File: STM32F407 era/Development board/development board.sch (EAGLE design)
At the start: 59 parts, among them IC1 74HC595N, IC2 74HC595N, IC3 317T, IC4 317T, X1 K375M, X2 HD44780LCD-1602, X3 SDBMF

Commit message: Continued work on dev board layout
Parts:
- added H1, H2, H3: MOUNT-HOLE3.2, holes:MOUNT-HOLE3.2
- added ISP1: AVRISP-BOX, adafruit:AVRISP-BOX
- added JP1: USB_MICROB_PLUGCONN-11752, SparkFun-Connectors:USB_MICROB_PLUGCONN-11752
- added JP2: (no value), microbuilder:HEADER-1X2ROUND
- added R28: 1k8, microbuilder:RESISTOR_0603
- added SV1: (no value), con-lstb:MA08-1
- added SV2, SV3, SV4: (no value), con-lstb:MA03-1
- added U$57: MICROFIT4, unicorn:MICROFIT4
- added U1: MAX13052ESA+, Maxim_By_element14_Batch_1:MAX13052ESA+
- added X4, X8, X9: 057-006-1, con-panduit:057-006-1
- R2: value (none) -> 732
- R4: value (none) -> 400
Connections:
- removed net N$20: U$1G$3.PB7
- removed net N$33: U$1G$2.PB12
- new net CANH: R28.2, U$57.PIN1, U1.CANH
- new net CANL: R28.1, U$57.PIN2, U1.CANL
- new net CAN_RX: U$1G$3.PB5, U1.TXD
- new net CAN_TX: U$1G$3.PB6, U1.RXD
- new net D+: JP1.D+, U$1G$2.PB15
- new net D-: JP1.D-, U$1G$2.PB14
- new net DAC: JP2.2, U$1G$1.PA4
- new net SCL: SV4.2, U$1G$3.PB8, X9-3.S, X9-4.S
- new net SDA: SV4.1, U$1G$3.PB7, X9-5.S, X9-6.S
- new net SHIFTREG_LATCH: IC1A.RCK, IC2A.RCK
- new net SPI_MISO: ISP1.MISO, U$1G$1.PA6
- new net SPI_MOSI: IC1A.SER, ISP1.MOSI, U$1G$1.PA7
- new net SPI_SCK: IC1A.SCK, IC2A.SCK, ISP1.SCK, U$1G$1.PA5
- new net USART1_RX: SV2.2, U$1G$1.PB11, X4-3.S, X4-4.S
- new net USART1_TX: SV2.1, U$1G$1.PB10, X4-5.S, X4-6.S
- new net USART2_RX: SV3.2, U$1G$3.PD6, X8-3.S, X8-4.S
- new net USART2_TX: SV3.1, U$1G$3.PD5, X8-5.S, X8-6.S
- net 3.3V: now also IC1A.SCL, IC2A.SCL, ISP1.VCC, U1.VCC
- net E: now also U$1G$2.PC7; no longer U$1G$2.PB15
- net GND: now also IC1A.G, IC2A.G, ISP1.GND, JP1.GND, JP1.SHIELD, JP2.1, SV2.3, SV3.3, SV4.3, U$57.PIN3, U$57.PIN4, U1.GND, U1.RS, X4-1.S, X4-2.S, X8-1.S, X8-2.S, X9-1.S, X9-2.S
- net LED1: now also SV1.1, U$1G$1.PC4
- net LED2: now also SV1.2, U$1G$1.PC5
- net LED3: now also SV1.3, U$1G$1.PB0
- net LED4: now also SV1.4, U$1G$1.PB1
- net LED5: now also SV1.5, U$1G$1.PE7
- net LED6: now also SV1.6, U$1G$1.PA3
- net LED7: now also SV1.7, U$1G$2.PB12
- net LED8: now also SV1.8, U$1G$2.PA8
- net RW: now also U$1G$2.PC6; no longer U$1G$2.PB14
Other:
- note added: "DAC"
- note added: "I2C"
- note added: "USART1"
- note added: "USART2"
- moved on the sheet: C1, DIS2, IC2, IC2P, R5

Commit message: updates to the layout and done routing (maybe)
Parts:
- added JP3: (no value), pinhead:PINHD-2X11
- added LED10, LED9: (no value), led:LED3MM
- added R29: 150, microbuilder:RESISTOR_0603
- added R30: 100, microbuilder:RESISTOR_0603
- added SV5: (no value), con-lstb:MA03-2
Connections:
- new net N$20: LED10.A, R30.1
- new net N$31: LED9.A, R29.1
- new net PA0: JP3.4, U$1G$4.PA0
- new net PA1: JP3.3, U$1G$4.PA1
- new net PA2: JP3.2, U$1G$4.PA2
- new net PA9: JP3.1, U$1G$2.PA9
- new net PB4: JP3.18, U$1G$3.PB4
- new net PB9: JP3.17, U$1G$3.PB9
- new net PC0: JP3.8, U$1G$4.PC0
- new net PC1: JP3.7, U$1G$4.PC1
- new net PC13: JP3.9, U$1G$4.PC13
- new net PC2: JP3.6, U$1G$4.PC2
- new net PC3: JP3.5, U$1G$4.PC3
- new net PD4: JP3.20, U$1G$3.PD4
- new net PD7: JP3.19, U$1G$3.PD7
- new net PE0: JP3.16, U$1G$3.PE0
- new net PE1: JP3.15, U$1G$3.PE1
- new net PE2: JP3.14, U$1G$4.PE2
- new net PE3: JP3.13, U$1G$4.PE3
- new net PE4: JP3.12, U$1G$4.PE4
- new net PE5: JP3.11, U$1G$4.PE5
- new net PE6: JP3.10, U$1G$4.PE6
- net 3.3V: now also R30.2, SV5.2
- net 5.0V: now also R29.2
- net GND: now also JP3.21, JP3.22, LED10.C, LED9.C, SV5.6
- net SPI_MISO: now also SV5.1
- net SPI_MOSI: now also SV5.4
- net SPI_SCK: now also SV5.3
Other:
- moved on the sheet: C1, C2, C3, C4, C5, C6, DIS1, DIS2, IC1, IC1P, IC2, IC2P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

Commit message: fixed errors on dev board
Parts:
- removed JP1: USB_MICROB_PLUGCONN-11752, SparkFun-Connectors:USB_MICROB_PLUGCONN-11752
- added X5: PN61729-S, con-berg:PN61729-S
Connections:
- removed net SHIFTREG_LATCH: IC1A.RCK, IC2A.RCK
- net D+: now also X5.3; no longer JP1.D+
- net D-: now also X5.2; no longer JP1.D-
- net GND: now also X3.3, X5.4, X5.S1, X5.S2; no longer JP1.GND, JP1.SHIELD, X3.9
- net PA9: now also IC1A.RCK, IC2A.RCK
- net SDIO_CMD: now also R7.1, X3.2; no longer R8.1, X3.3
- net SDIO_D0: now also R8.1; no longer R9.1
- net SDIO_D1: now also R9.1; no longer R10.1
- net SDIO_D2: now also R10.1, X3.9; no longer R6.1, X3.1
- net SDIO_D3: now also R6.1, X3.1; no longer R7.1, X3.2

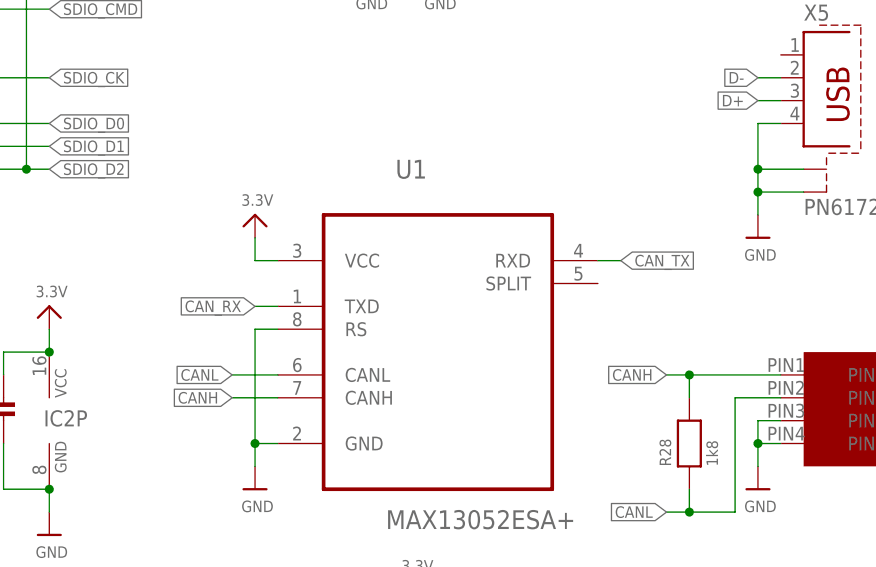
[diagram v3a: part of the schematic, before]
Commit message: fixed CAN controller connections
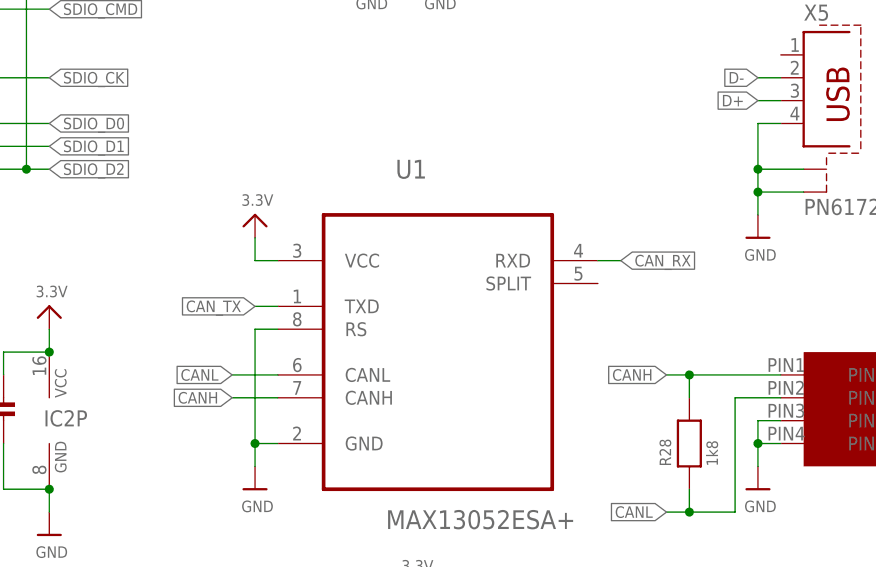
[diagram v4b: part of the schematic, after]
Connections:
- net CAN_RX: now also U1.RXD; no longer U1.TXD
- net CAN_TX: now also U1.TXD; no longer U1.RXD
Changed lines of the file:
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@@
 </segment>
 <segment>
-<pinref part="U1" gate="A" pin="TXD"/>
-<wire x1="203.2" y1="-48.26" x2="200.66" y2="-48.26" width="0.1524" layer="91"/>
-<label x="200.66" y="-48.26" size="1.27" layer="95" rot="R180" xref="yes"/>
+<pinref part="U1" gate="A" pin="RXD"/>
+<wire x1="238.76" y1="-43.18" x2="241.3" y2="-43.18" width="0.1524" layer="91"/>
+<label x="241.3" y="-43.18" size="1.27" layer="95" xref="yes"/>
 </segment>
 </net>
@@
 </segment>
 <segment>
-<pinref part="U1" gate="A" pin="RXD"/>
-<wire x1="238.76" y1="-43.18" x2="241.3" y2="-43.18" width="0.1524" layer="91"/>
-<label x="241.3" y="-43.18" size="1.27" layer="95" xref="yes"/>
+<pinref part="U1" gate="A" pin="TXD"/>
+<wire x1="203.2" y1="-48.26" x2="200.66" y2="-48.26" width="0.1524" layer="91"/>
+<label x="200.66" y="-48.26" size="1.27" layer="95" rot="R180" xref="yes"/>
 </segment>
 </net>

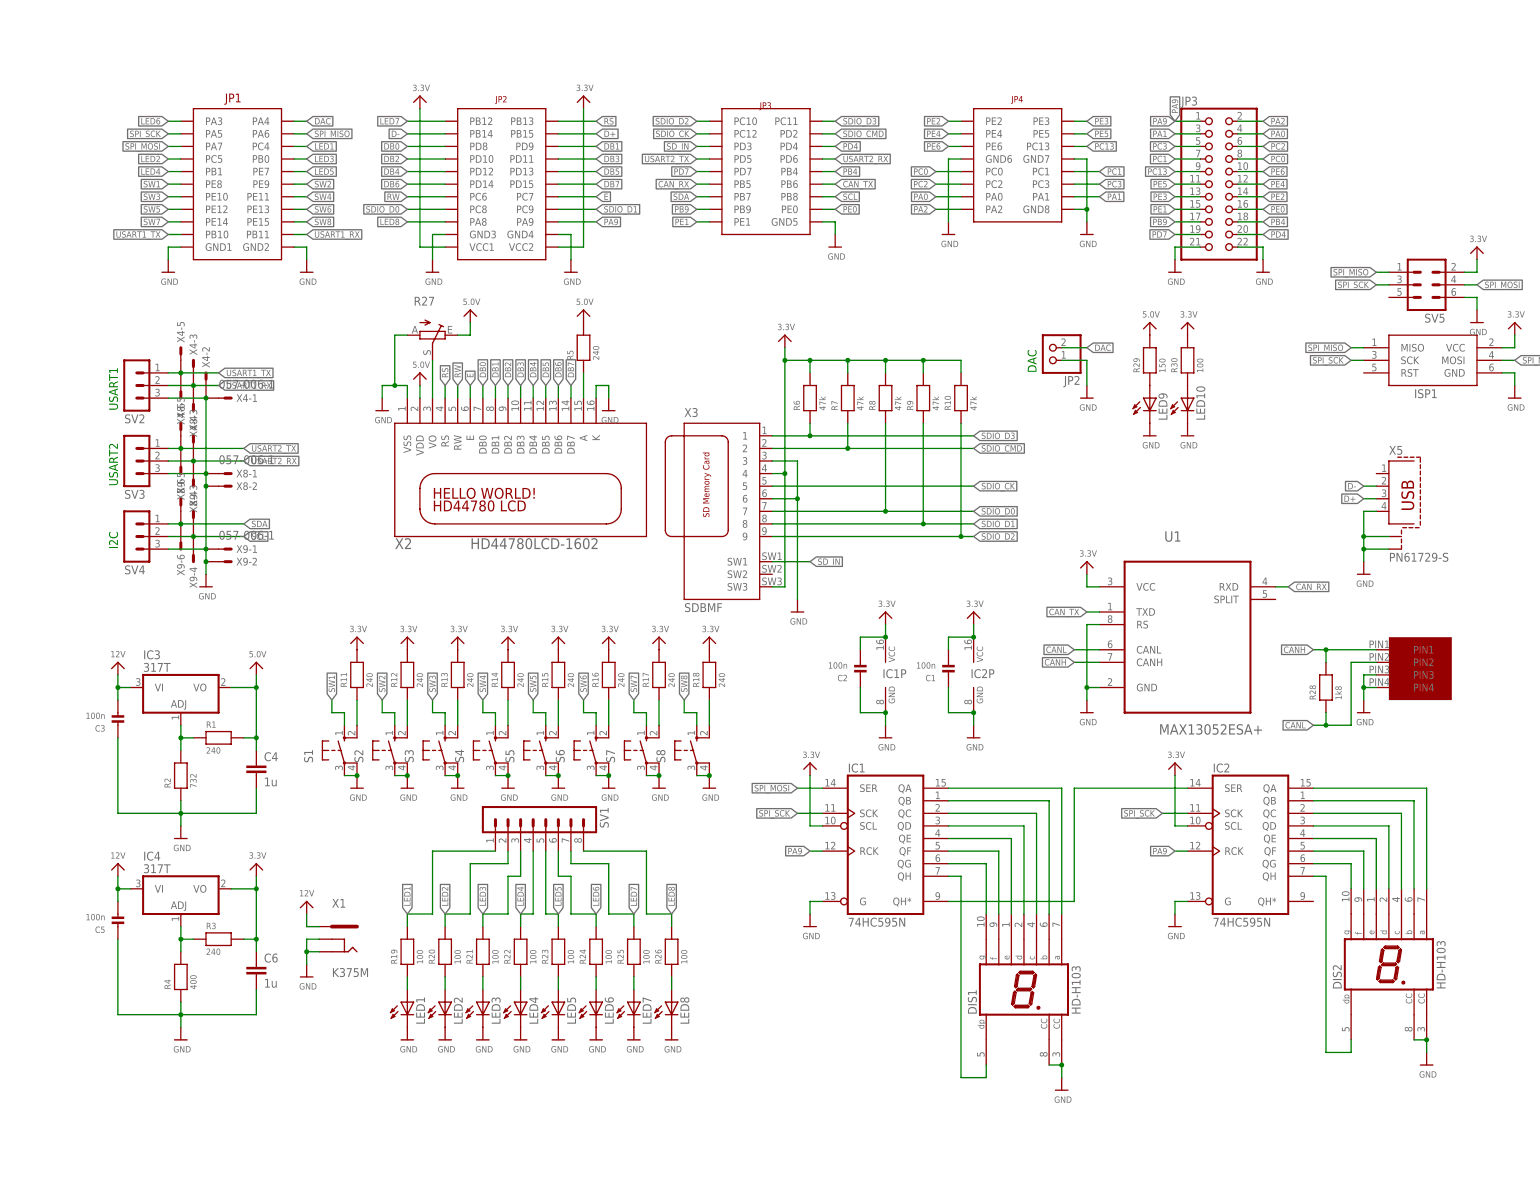
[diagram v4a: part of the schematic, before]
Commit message: fixed CPU board header in library and dev board
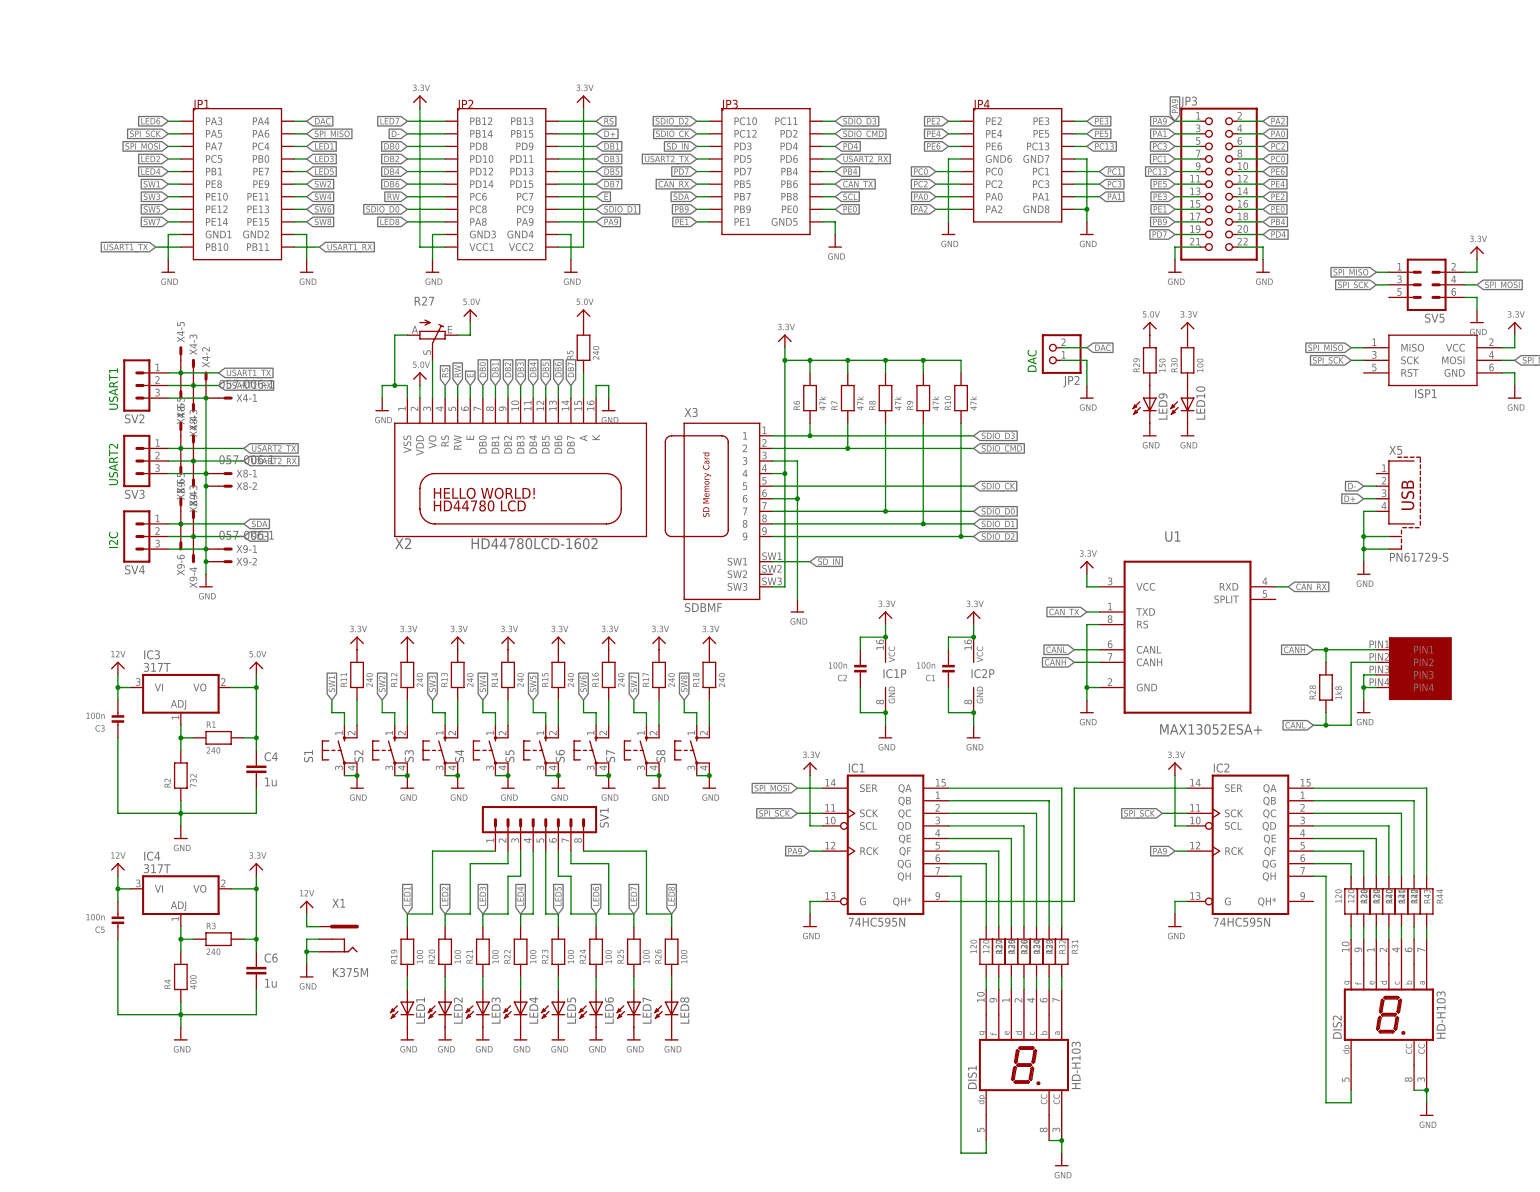
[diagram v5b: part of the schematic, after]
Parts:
- added R31, R32, R33, R34, R35, R36, R37, R38, R39, R40, R41, R42, R43, R44: 120, microbuilder:RESISTOR_0603
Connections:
- new net N$51: DIS1.A, R31.2
- new net N$52: DIS1.B, R32.2
- new net N$60: DIS1.C, R33.2
- new net N$61: DIS1.D, R34.2
- new net N$62: DIS1.F, R35.2
- new net N$63: DIS1.E, R36.2
- new net N$64: DIS1.G, R37.2
- new net N$65: DIS2.G, R38.2
- new net N$66: DIS2.F, R39.2
- new net N$67: DIS2.E, R40.2
- new net N$68: DIS2.D, R41.2
- new net N$69: DIS2.C, R42.2
- new net N$70: DIS2.B, R43.2
- new net N$71: DIS2.A, R44.2
- net N$11: now also R37.1; no longer DIS1.G
- net N$12: now also R35.1; no longer DIS1.F
- net N$13: now also R36.1; no longer DIS1.E
- net N$14: now also R34.1; no longer DIS1.D
- net N$15: now also R33.1; no longer DIS1.C
- net N$16: now also R32.1; no longer DIS1.B
- net N$17: now also R31.1; no longer DIS1.A
- net N$2: now also R38.1; no longer DIS2.G
- net N$3: now also R39.1; no longer DIS2.F
- net N$4: now also R40.1; no longer DIS2.E
- net N$5: now also R41.1; no longer DIS2.D
- net N$6: now also R42.1; no longer DIS2.C
- net N$7: now also R43.1; no longer DIS2.B
- net N$8: now also R44.1; no longer DIS2.A
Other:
- moved on the sheet: DIS1, DIS2
